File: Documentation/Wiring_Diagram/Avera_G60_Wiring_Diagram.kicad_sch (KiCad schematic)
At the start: 9 parts

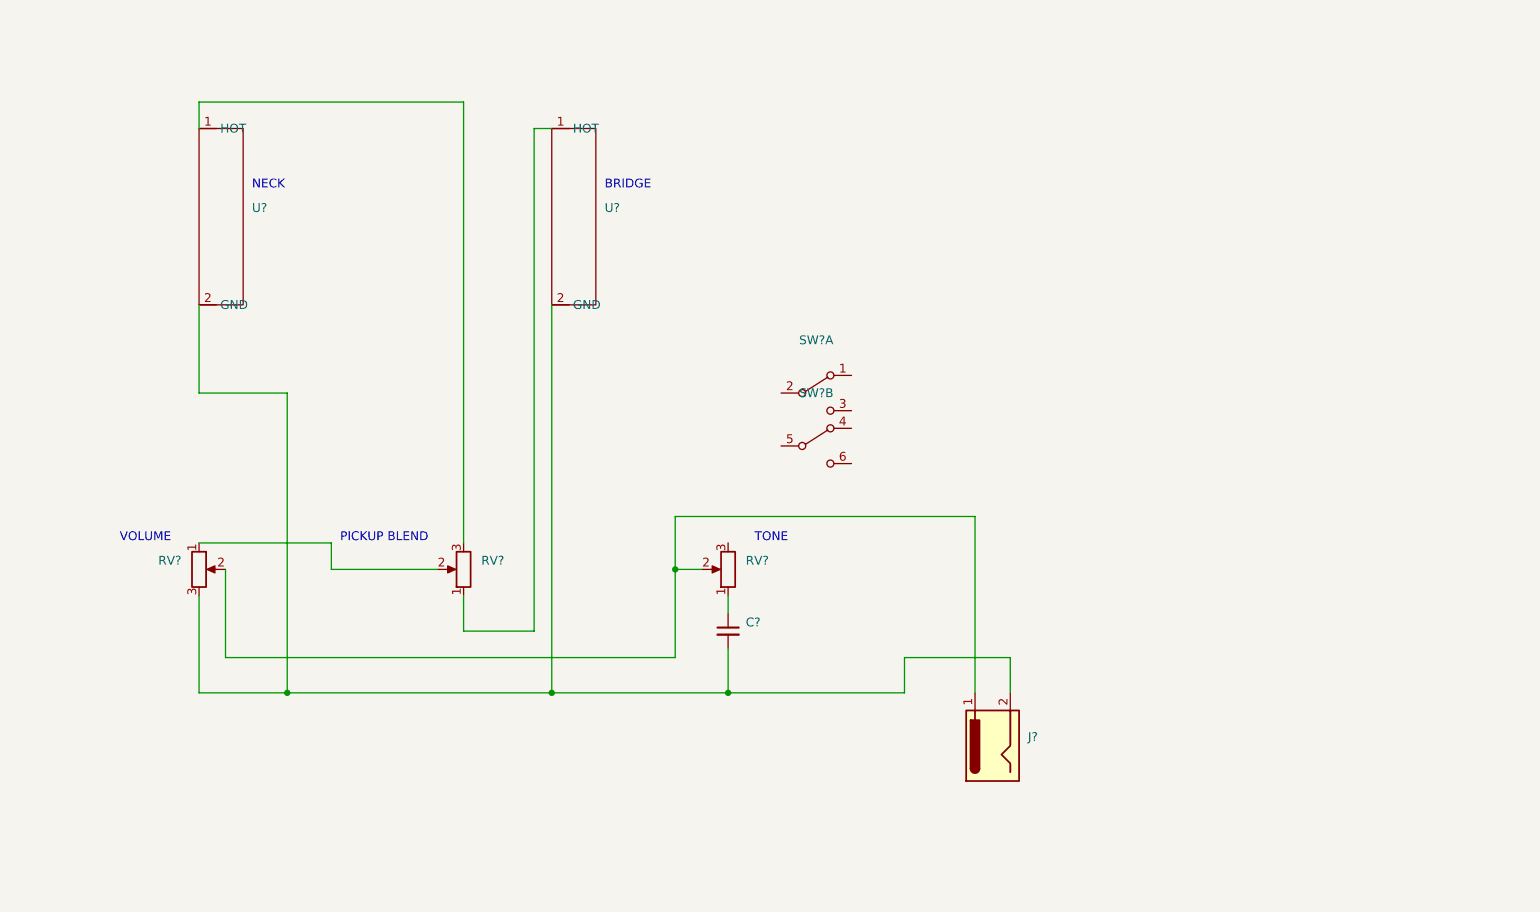
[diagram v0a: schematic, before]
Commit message: add renders, move out blender files (too large)
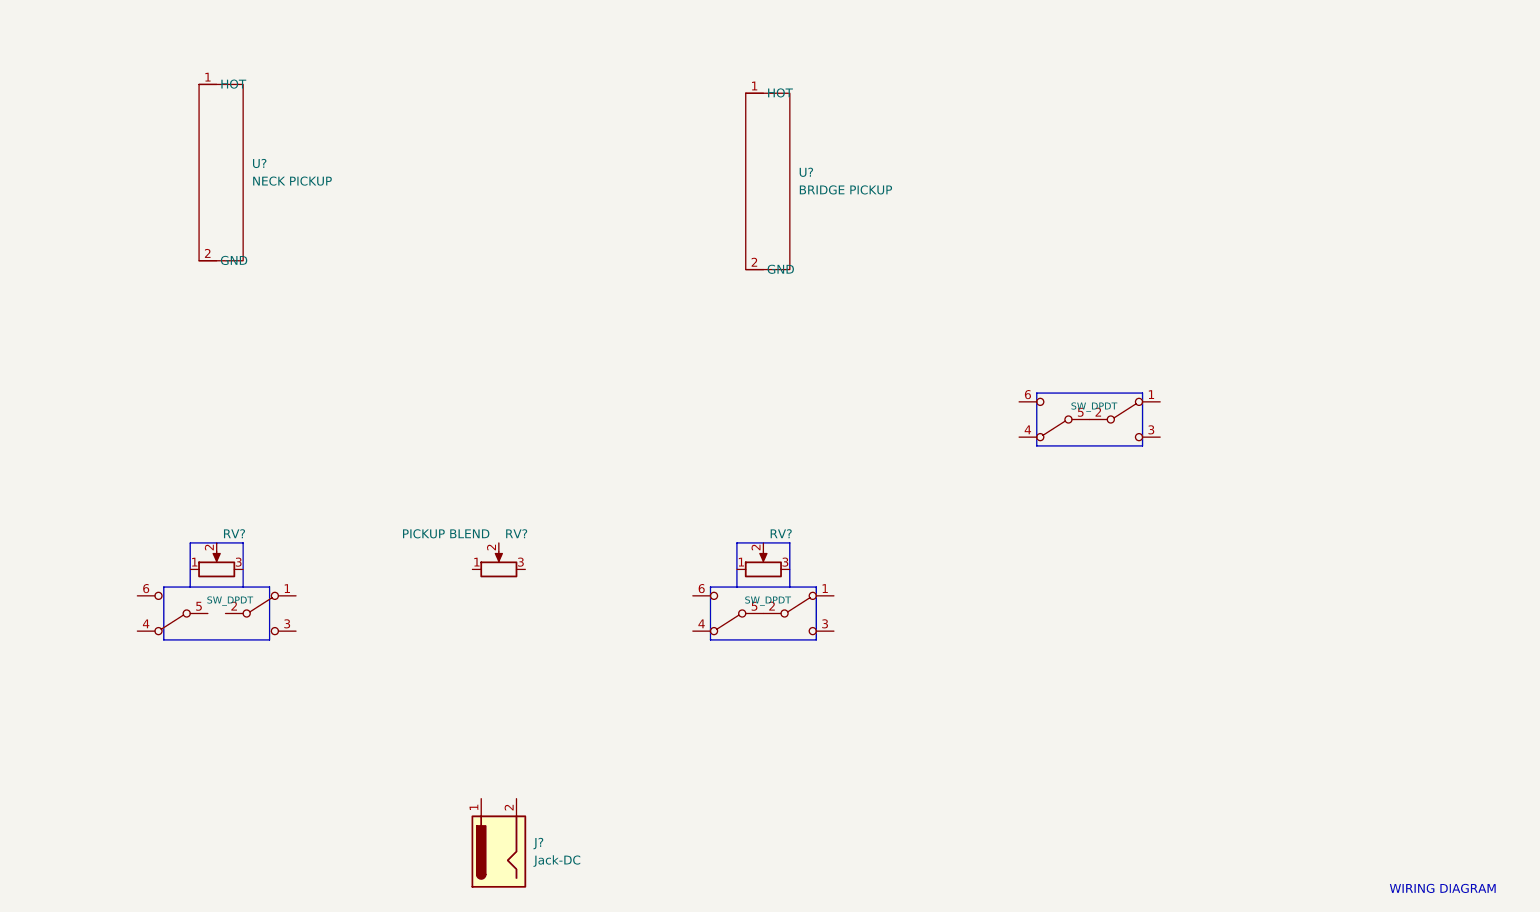
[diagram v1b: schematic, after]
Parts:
- removed C?: (no value), symbol Device:C_Small
- removed RV? (x2): (no value), symbol Device:R_Potentiometer
- added RV? (x2): (no value), symbol Device:R_Potentiometer
- added SW? (x2): SW_DPDT, symbol Switch:SW_DPDT_x2
- added SW? (x2): SW_DPDT_x2, symbol Switch:SW_DPDT_x2
- J?: value (none) -> Jack-DC
- RV?: value (none) -> PICKUP BLEND
- SW?: value (none) -> SW_DPDT
- SW?: value (none) -> SW_DPDT_x2
- U?: value (none) -> BRIDGE PICKUP
- U?: value (none) -> NECK PICKUP
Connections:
- net at SW?.2 (B): now also SW?.5 (B)
- net at U?.1 (HOT): no longer RV?.1
- net at U?.1 (HOT): no longer RV?.3
- new net: SW?.2 (B), SW?.5 (B)
- now unconnected: J?.2, U?.2 (GND), U?.2 (GND)
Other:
- note added: "WIRING DIAGRAM"
- note removed: "BRIDGE"
- note removed: "NECK"
- note removed: "PICKUP BLEND"
- note removed: "TONE"
- note removed: "VOLUME"
- moved on the sheet: J?, RV?, U?

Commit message: set up all wiring diagram connections
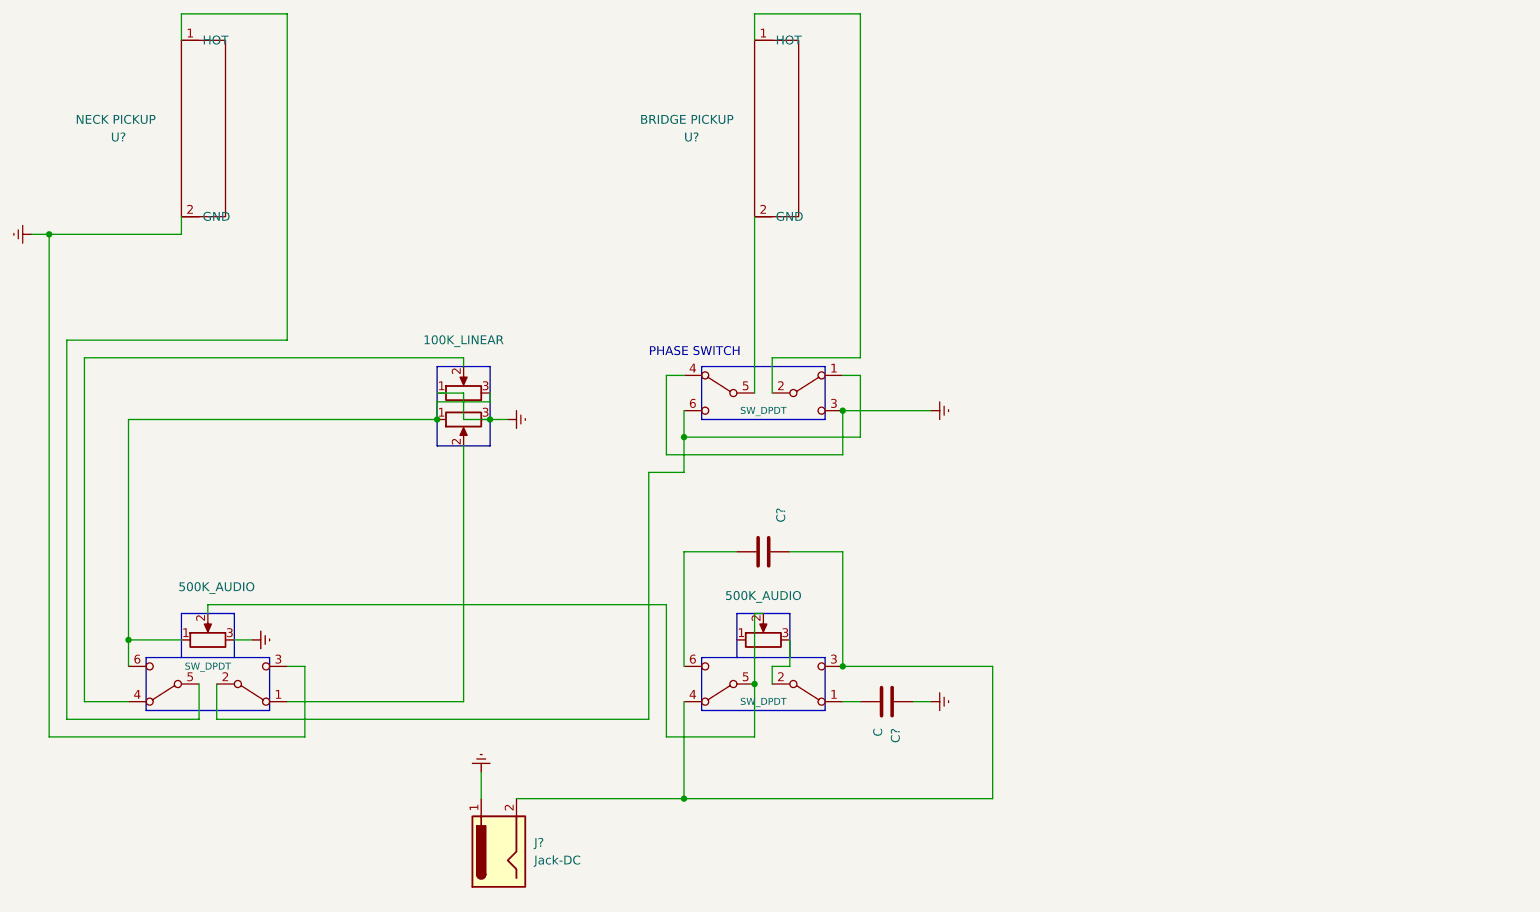
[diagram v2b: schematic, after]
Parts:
- added C?: C, symbol Device:C
- added C?: (no value), symbol Device:C
- added RV?: (no value), symbol Device:R_Potentiometer
- 100K_LINEAR: renamed from RV?; value PICKUP BLEND -> (none)
- gave numbers to parts that had none: 1
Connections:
- net at SW?.1 (A): now also SW?.2 (B), SW?.6 (C)
- net at SW?.2 (B): now also U?.1 (HOT); no longer SW?.5 (B)
- net Earth: now reaches SW?.3 (C)
- net Earth: now also 100K_LINEAR.1, 500K_AUDIO.3, J?.1, SW?.3 (C), SW?.4 (A), U?.2 (GND), C?.1, RV?.3
- net at J?.2: now also SW?.3 (C), SW?.4 (A), C?.1
- net at SW?.1 (A): now also C?.2
- net at SW?.2 (B): now also 500K_AUDIO.3; no longer SW?.5 (B)
- net at U?.2 (GND): now also SW?.5 (B)
- net at U?.1 (HOT): now also SW?.5 (B)
- net at SW?.1 (A): now also RV?.2
- net at 100K_LINEAR.2: now also SW?.4 (A)
- net at 100K_LINEAR.3: now also 500K_AUDIO.1, SW?.6 (C), RV?.1
- net at SW?.6 (C): now also C?.2
- net at 500K_AUDIO.2: now also 500K_AUDIO.2, SW?.5 (B)
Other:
- note added: "PHASE SWITCH"
- note removed: "WIRING DIAGRAM"
- moved on the sheet: 100K_LINEAR, 500K_AUDIO, U?
